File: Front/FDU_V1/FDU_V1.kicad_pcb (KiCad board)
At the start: 4 copper layers, 197.1 x 120.1 mm, 165 parts, among them IC1 SN65HVD230, IC10 XL1509-5.0E1, IC11 TDA2822D, IC12 AMS1117-3.3, IC2 WeMos_D1_mini, IC3 74LVC3G17DC,125, IC4 STM32F103RBT6, IC5 MCP6291T-E_OT, IC6 LM2901, IC7 CD74HC30M96, IC8 74LVC3G17DC,125, IC9 SN74LVC3G04DCUR, J1 SWPROG, X1 S3D4.000000B20F30T, Y1 8MHz

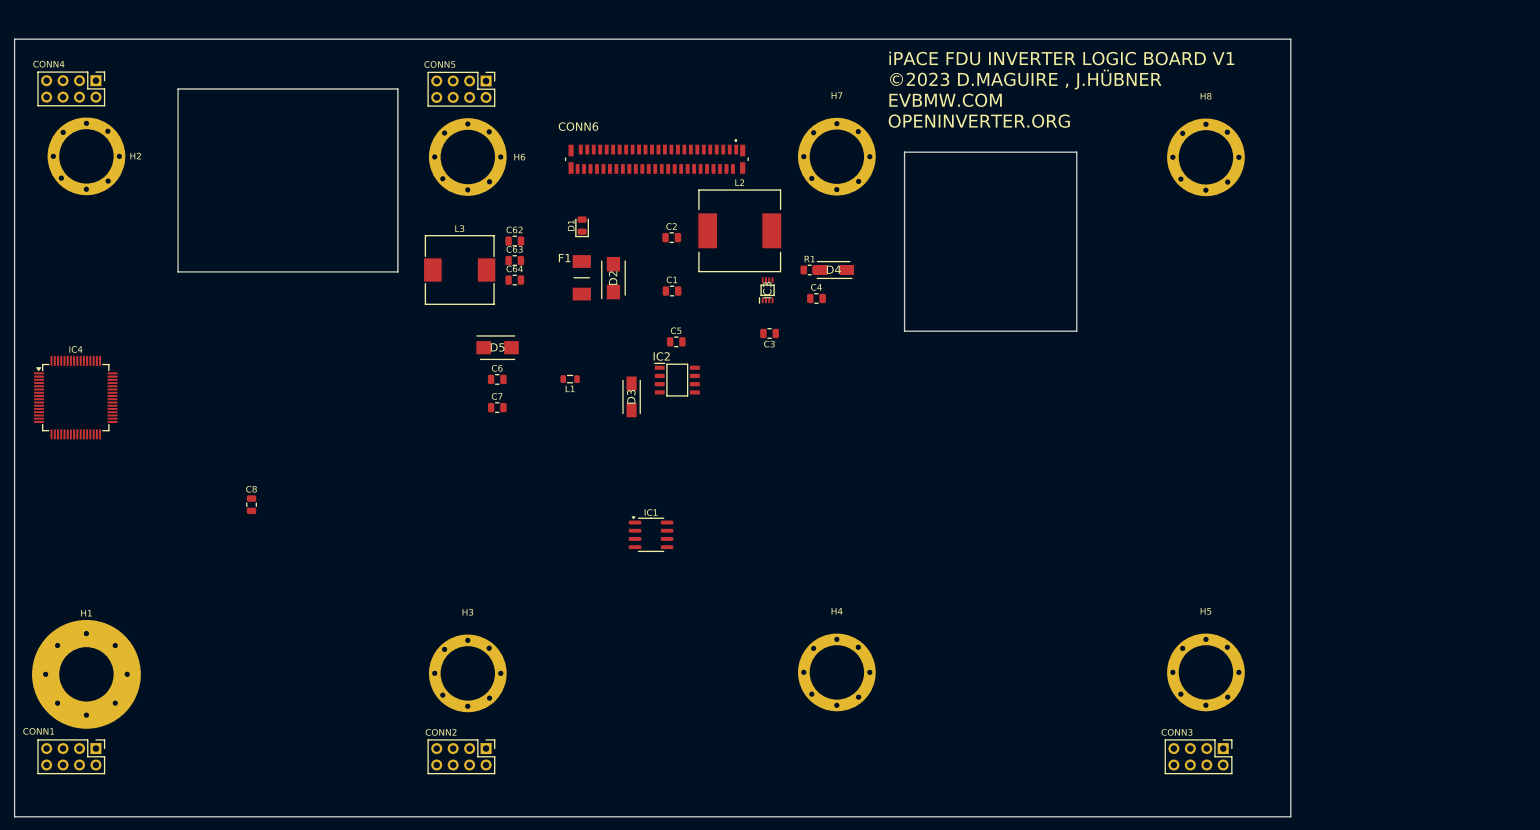
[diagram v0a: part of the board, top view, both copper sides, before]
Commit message: Continued work on both schematic and board placement.
Schematic: Pinout added for external 28pin connector.
PCB: Corrected board outline dimensions and all external dependencies. (holes, pin headers, ZIP connector)
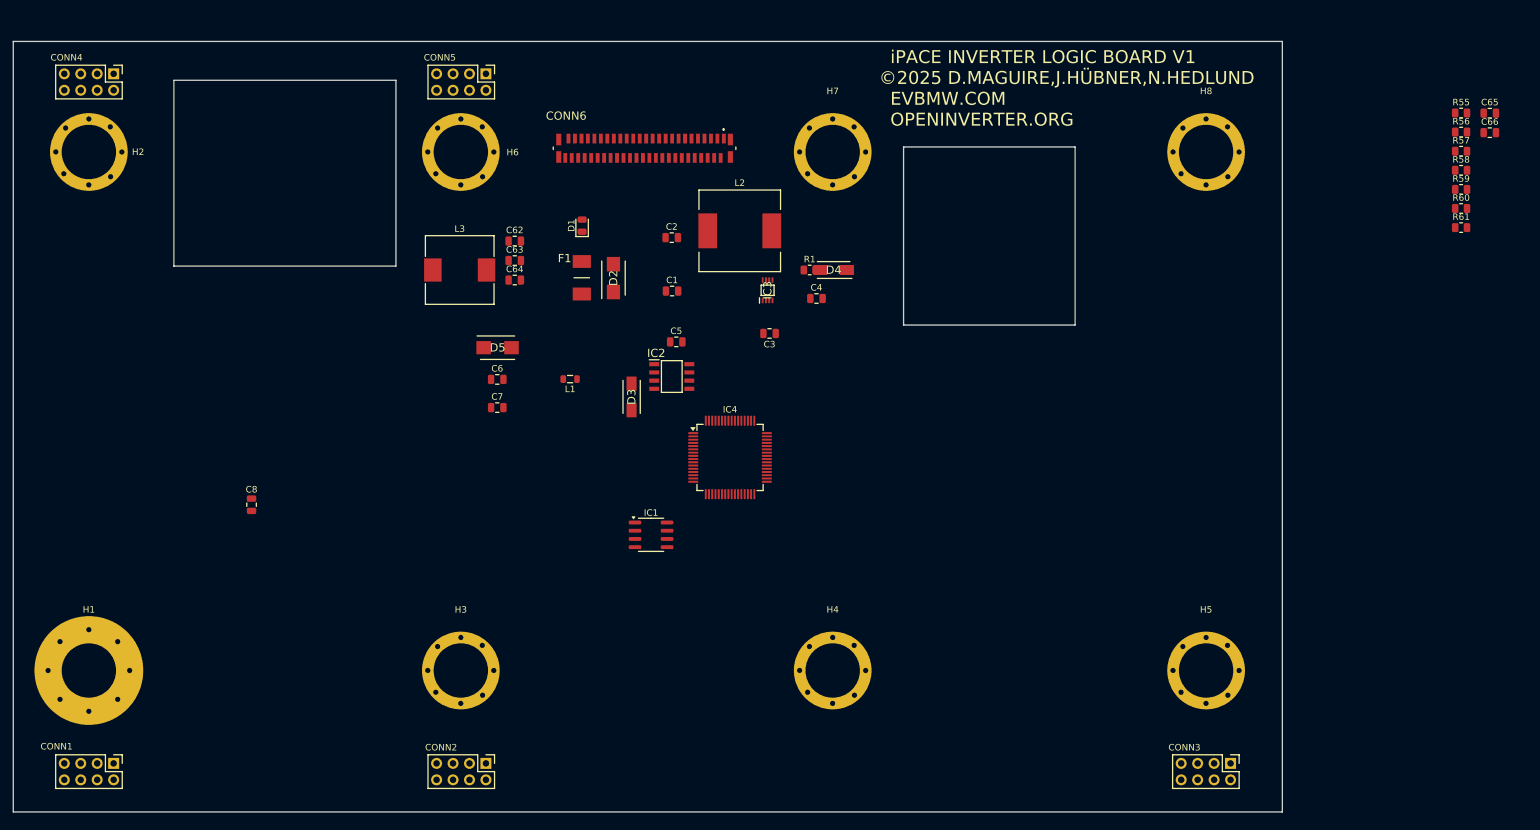
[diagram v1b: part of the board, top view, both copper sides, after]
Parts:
- added C65: 1uF, Capacitor_SMD:C_0805_2012Metric, F.Cu at (278.0, 51.1)
- added C66: 1uF, Capacitor_SMD:C_0805_2012Metric, F.Cu at (278.0, 54.1)
- added R55: 1.2K, Resistor_SMD:R_0805_2012Metric, F.Cu at (273.6, 51.0)
- added R56: 1.2K, Resistor_SMD:R_0805_2012Metric, F.Cu at (273.6, 54.0)
- added R57: 2.2K, Resistor_SMD:R_0805_2012Metric, F.Cu at (273.6, 57.0)
- added R58: 1.2K, Resistor_SMD:R_0805_2012Metric, F.Cu at (273.6, 59.9)
- added R59: 0K, Resistor_SMD:R_0805_2012Metric, F.Cu at (273.6, 62.9)
- added R60: 1.2K, Resistor_SMD:R_0805_2012Metric, F.Cu at (273.6, 65.8)
- added R61: 2.2K, Resistor_SMD:R_0805_2012Metric, F.Cu at (273.6, 68.8)
- moved IC4 101.5 mm to (160.7, 104.2)
- moved CONN1 3.56 mm to (65.5, 151.5)
- moved CONN4 2.93 mm to (65.5, 45.0)
- moved CONN3 2.55 mm to (238.0, 151.5)
- moved CONN6 2.55 mm to (147.5, 56.5)
- moved CONN2 2.29 mm to (123.0, 151.5)
- moved H6 1.33 mm to (119.1, 57.1)
- moved H3 1.16 mm to (119.1, 137.2)
- moved CONN5 1.11 mm to (123.0, 45.0)
- moved IC2 1.01 mm to (151.7, 91.8)
- moved H7 0.97 mm to (176.6, 57.1)
- moved H8 0.83 mm to (234.2, 57.1)
- moved H2 0.77 mm to (61.7, 57.1)
- moved H4 0.71 mm to (176.6, 137.2)
- moved H1 0.70 mm to (61.7, 137.2)
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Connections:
- C34 pad 2: /EXCITER -> /EXCA
- C63 pad 1: /TMPM_IN -> /TMPM1_IN
- CONN6 pad 1: unconnected-(CONN6-Pad1) -> /CANH
- CONN6 pad 10: unconnected-(CONN6-Pad10) -> /MOT_TMP1_2
- CONN6 pad 11: unconnected-(CONN6-Pad11) -> /MOT_TMP2_1
- CONN6 pad 12: unconnected-(CONN6-Pad12) -> /MOT_TMP2_2
- CONN6 pad 14: unconnected-(CONN6-Pad14) -> /BRAKE
- CONN6 pad 15: unconnected-(CONN6-Pad15) -> /THROTTLE 1
- CONN6 pad 16: unconnected-(CONN6-Pad16) -> /THROTTLE 2
- CONN6 pad 17: unconnected-(CONN6-Pad17) -> /EXCA
- CONN6 pad 18: unconnected-(CONN6-Pad18) -> /EXCB
- CONN6 pad 2: unconnected-(CONN6-Pad2) -> /CANL
- CONN6 pad 20: unconnected-(CONN6-Pad20) -> /RES_COSB
- CONN6 pad 21: unconnected-(CONN6-Pad21) -> /RES_COSA
- CONN6 pad 22: unconnected-(CONN6-Pad22) -> /CRUISE
- CONN6 pad 23: unconnected-(CONN6-Pad23) -> /RES_SINA
- CONN6 pad 24: unconnected-(CONN6-Pad24) -> /RES_SINB
- CONN6 pad 28: unconnected-(CONN6-Pad28) -> +12P
- CONN6 pad 29: unconnected-(CONN6-Pad29) -> +12P
- CONN6 pad 3: unconnected-(CONN6-Pad3) -> /START
- CONN6 pad 30: unconnected-(CONN6-Pad30) -> +12P
- CONN6 pad 31: unconnected-(CONN6-Pad31) -> +12P
- CONN6 pad 32: unconnected-(CONN6-Pad32) -> +12P
- CONN6 pad 33: unconnected-(CONN6-Pad33) -> +12P
- CONN6 pad 34: unconnected-(CONN6-Pad34) -> +12P
- CONN6 pad 35: unconnected-(CONN6-Pad35) -> +12P
- CONN6 pad 36: unconnected-(CONN6-Pad36) -> +12P
- CONN6 pad 37: unconnected-(CONN6-Pad37) -> +12P
- CONN6 pad 38: unconnected-(CONN6-Pad38) -> +12P
- CONN6 pad 39: unconnected-(CONN6-Pad39) -> +12P
- CONN6 pad 40: unconnected-(CONN6-Pad40) -> +12P
- CONN6 pad 41: unconnected-(CONN6-Pad41) -> +12P
- CONN6 pad 42: unconnected-(CONN6-Pad42) -> +12P
- CONN6 pad 43: unconnected-(CONN6-Pad43) -> +12P
- CONN6 pad 44: unconnected-(CONN6-Pad44) -> +12P
- CONN6 pad 45: unconnected-(CONN6-Pad45) -> +12P
- CONN6 pad 46: unconnected-(CONN6-Pad46) -> +12P
- CONN6 pad 47: unconnected-(CONN6-Pad47) -> +12P
- CONN6 pad 48: unconnected-(CONN6-Pad48) -> +12P
- CONN6 pad 49: unconnected-(CONN6-Pad49) -> +12P
- CONN6 pad 5: unconnected-(CONN6-Pad5) -> /WTR_TMP1
- CONN6 pad 50: unconnected-(CONN6-Pad50) -> +12P
- CONN6 pad 6: unconnected-(CONN6-Pad6) -> /WTR_TMP2
- CONN6 pad 7: unconnected-(CONN6-Pad7) -> /FORWARD
- CONN6 pad 8: unconnected-(CONN6-Pad8) -> /REVERSE
- CONN6 pad 9: unconnected-(CONN6-Pad9) -> /MOT_TMP1_1
- D12 pad 1: /TMPM_IN -> /TMPM1_IN
- R50 pad 2: /MOT_TMP1 -> /MOT_TMP1_1
- R51 pad 1: /TMPM_IN -> /TMPM1_IN
- R51 pad 2: /MOT_TMP2 -> /MOT_TMP1_2
- R52 pad 1: /TMPM_IN -> /TMPM1_IN
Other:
- board size 197.1 x 120.1 mm -> 196 x 119 mm
- board text added: "iPACE INVERTER LOGIC BOARD V1 ©2025 D.MAGUIRE,J.HÜBNER,N.HEDLUND EVBMW.COM OPENINVERTER.ORG"
- board text removed: "iPACE FDU INVERTER LOGIC BOARD V1 ©2023 D.MAGUIRE , J.HÜBNER EVBMW.COM OPENINVERTER.ORG"
